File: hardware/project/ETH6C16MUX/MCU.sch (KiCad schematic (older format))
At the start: 32 parts

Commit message: Schematic design
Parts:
- U?: symbol ETH6C12MUX:STM32F765ZGT6 -> ETH6C16MUX:STM32F765ZGT6
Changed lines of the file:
@@
 EESchema Schematic File Version 4
-LIBS:ETH6C12MUX-cache
+LIBS:ETH6C16MUX-cache
 EELAYER 30 0
 EELAYER END
@@
 	7600 10900 7600 10950
 $Comp
-L ETH6C12MUX:+3.3V_MCU #PWR?
+L ETH6C16MUX:+3.3V_MCU #PWR?
 U 1 1 5DA5C116
 P 6700 10450
@@
 $EndComp
 $Comp
-L ETH6C12MUX:+3.3V_MCU #PWR?
+L ETH6C16MUX:+3.3V_MCU #PWR?
 U 1 1 5DBD22D5
 P 850 9200
@@
 $EndComp
 $Comp
-L ETH6C12MUX:+3.3V_MCU #PWR?
+L ETH6C16MUX:+3.3V_MCU #PWR?
 U 1 1 5DE7C3C1
 P 10750 9950
@@
 	3650 6000 2900 6000
 $Comp
-L ETH6C12MUX:+3.3V_MCU #PWR?
+L ETH6C16MUX:+3.3V_MCU #PWR?
 U 1 1 5DA689C0
 P 15150 7550
@@
 	9350 800  9350 850
 $Comp
-L ETH6C12MUX:+3.3V_MCU #PWR?
+L ETH6C16MUX:+3.3V_MCU #PWR?
 U 1 1 5DA4E816
 P 9350 800
@@
 $EndComp
 $Comp
-L ETH6C12MUX:STM32F765ZGT6 U?
+L ETH6C16MUX:STM32F765ZGT6 U?
 U 1 1 5D61C76C
 P 9350 4950
@@
 	8550 10450 8550 10500
 $Comp
-L ETH6C12MUX:+3.3V_MCU #PWR?
+L ETH6C16MUX:+3.3V_MCU #PWR?
 U 1 1 5DA61F58
 P 8550 10450
@@
 	3400 10450 3400 10500
 $Comp
-L ETH6C12MUX:+3.3V_MCU #PWR?
+L ETH6C16MUX:+3.3V_MCU #PWR?
 U 1 1 5DA55A02
 P 3400 10450
@@
 $EndComp
 $Comp
-L ETH6C12MUX:+3.3V_MCU #PWR?
+L ETH6C16MUX:+3.3V_MCU #PWR?
 U 1 1 5DEE379F
 P 1350 3850
@@
 	3500 8700 3650 8700
 $Comp
-L ETH6C12MUX:+3.3V_MCU #PWR?
+L ETH6C16MUX:+3.3V_MCU #PWR?
 U 1 1 5DCB5D39
 P 3150 8700
@@
 	1800 2850 1800 2750
 $Comp
-L ETH6C12MUX:+3.3V_MCU #PWR?
+L ETH6C16MUX:+3.3V_MCU #PWR?
 U 1 1 5DDA95AD
 P 1350 2150
@@
 $EndComp
 $Comp
-L ETH6C12MUX:+3.3V_MCU #PWR?
+L ETH6C16MUX:+3.3V_MCU #PWR?
 U 1 1 5DDAA87C
 P 1850 2850
@@
 I2C_SCL
 $Comp
-L ETH6C12MUX:+3.3V_MCU #PWR?
+L ETH6C16MUX:+3.3V_MCU #PWR?
 U 1 1 5DDCF30A
 P 1350 900

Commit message: FPGA schematic
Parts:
- removed U?: 24LC01, symbol Memory_EEPROM:24LC01
- added C? (x3): 100n, symbol Device:C
- added C?: 47n, symbol Device:C
- added U? (x2): S25FL064L_SOIC, symbol ETH6C16MUX:S25FL064L_SOIC
- added U?: ASDM1-20.000MHZ-LC-T, Oscillator:Oscillator_SMD_Abracon_ASDMB-4Pin_2.5x2.0mm, symbol Oscillator:ASDMB-xxxMHz
- U?: value MCP9804_MSOP -> MCP9804
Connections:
- net labels removed: MCU_SPI4_MISO, MCU_SPI4_MOSI, MCU_SPI4_NSS, MCU_SPI4_SCLK, MCU_SPI5_MISO, MCU_SPI5_NSS, MCU_SPI5_SCLK
- wire segments 206 -> 229
- no-connect marks 4 -> 5
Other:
- moved on the sheet: C?, D?, J?, R?, U?

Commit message: Schematic design
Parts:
- removed C?: 47n, symbol Device:C
- removed D?: LED_ARGB, symbol Device:LED_ARGB
- added D301: RED, symbol Device:LED
- added D302: GREEN, symbol Device:LED
- added D303: BLUE, symbol Device:LED
- added J303: Conn_02x01, Connector_PinHeader_2.54mm:PinHeader_1x02_P2.54mm_Vertical, symbol Connector_Generic:Conn_02x01
- added R301: 220, symbol Device:R
- added R302: 12k1, symbol Device:R
- added R303, R304: 4k7, symbol Device:R
- added R307, R308: 270, Resistor_SMD:R_0603_1608Metric_Pad1.05x0.95mm_HandSolder, symbol Device:R
- added R312: 10k, symbol Device:R
- C301, C302, C303, C306, C307, C308, C309, C310, C311, C312, C313, C314, C315, C316, C317, C318: renamed from C?; footprint (none) -> ETH6C16MXU:C_0603_A_Pad1.05x0.95mm_HandSolder
- J302: renamed from J?; footprint (none) -> Connector_PinHeader_2.54mm:PinHeader_1x02_P2.54mm_Vertical
- R306: renamed from R?; value R -> 270; footprint (none) -> Resistor_SMD:R_0603_1608Metric_Pad1.05x0.95mm_HandSolder
- R309, R310: renamed from R?; footprint (none) -> Resistor_SMD:R_0603_1608Metric_Pad1.05x0.95mm_HandSolder
- R311: renamed from R?; value 12k1 -> 10k
- U304: renamed from U?; footprint (none) -> Package_QFP:TQFP-144_20x20mm_P0.5mm
- gave numbers to parts that had none: 14
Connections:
- net labels added: +3.3V, FPGA1_CBSEL0, FPGA1_CBSEL1, FPGA1_CDONE, FPGA1_CFG_CS, FPGA1_CRESET_B, FPGA1_SPI5_CS, FPGA1_SPI5_MISO, FPGA1_SPI5_MOSI, FPGA1_SPI5_SLCK, FPGA2_CBSEL0, FPGA2_CBSEL1, FPGA2_CDONE, FPGA2_CFG_CS, FPGA2_CRESET_B, FPGA2_SPI4_CS, FPGA2_SPI4_MISO, FPGA2_SPI4_MOSI, FPGA2_SPI4_SLCK, MCU_DEFAULT, MODULE_DETECT
- net labels removed: +3.3V_MCU, FPGA_CBSEL0, FPGA_CBSEL1, FPGA_CDONE, FPGA_CFG_CS, FPGA_CRESET_B, FPGA_SPI3_CS
- wire segments 229 -> 271
- no-connect marks 5 -> 69
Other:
- moved on the sheet: C301, C302, C303, C304, C305, C319, C320, C321, C322, FB301, FB302, J301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

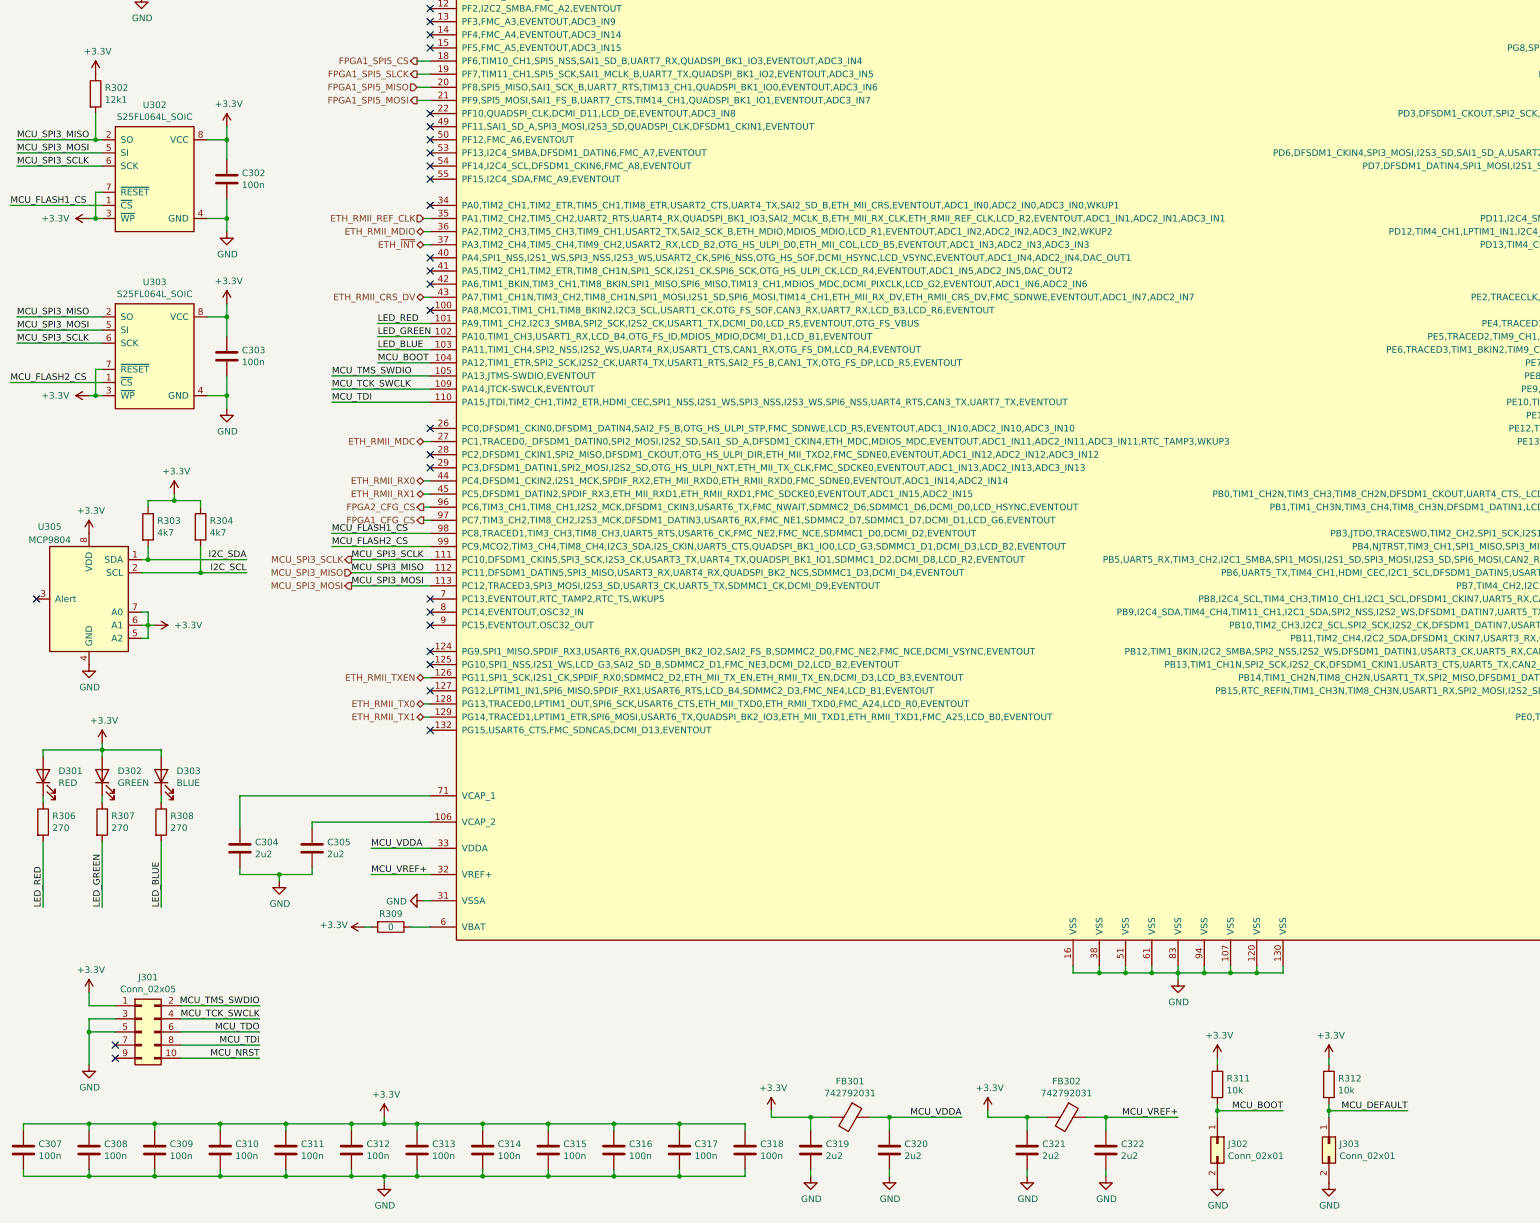
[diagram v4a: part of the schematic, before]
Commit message: PCB design, need to redesign of the board to board connectors.
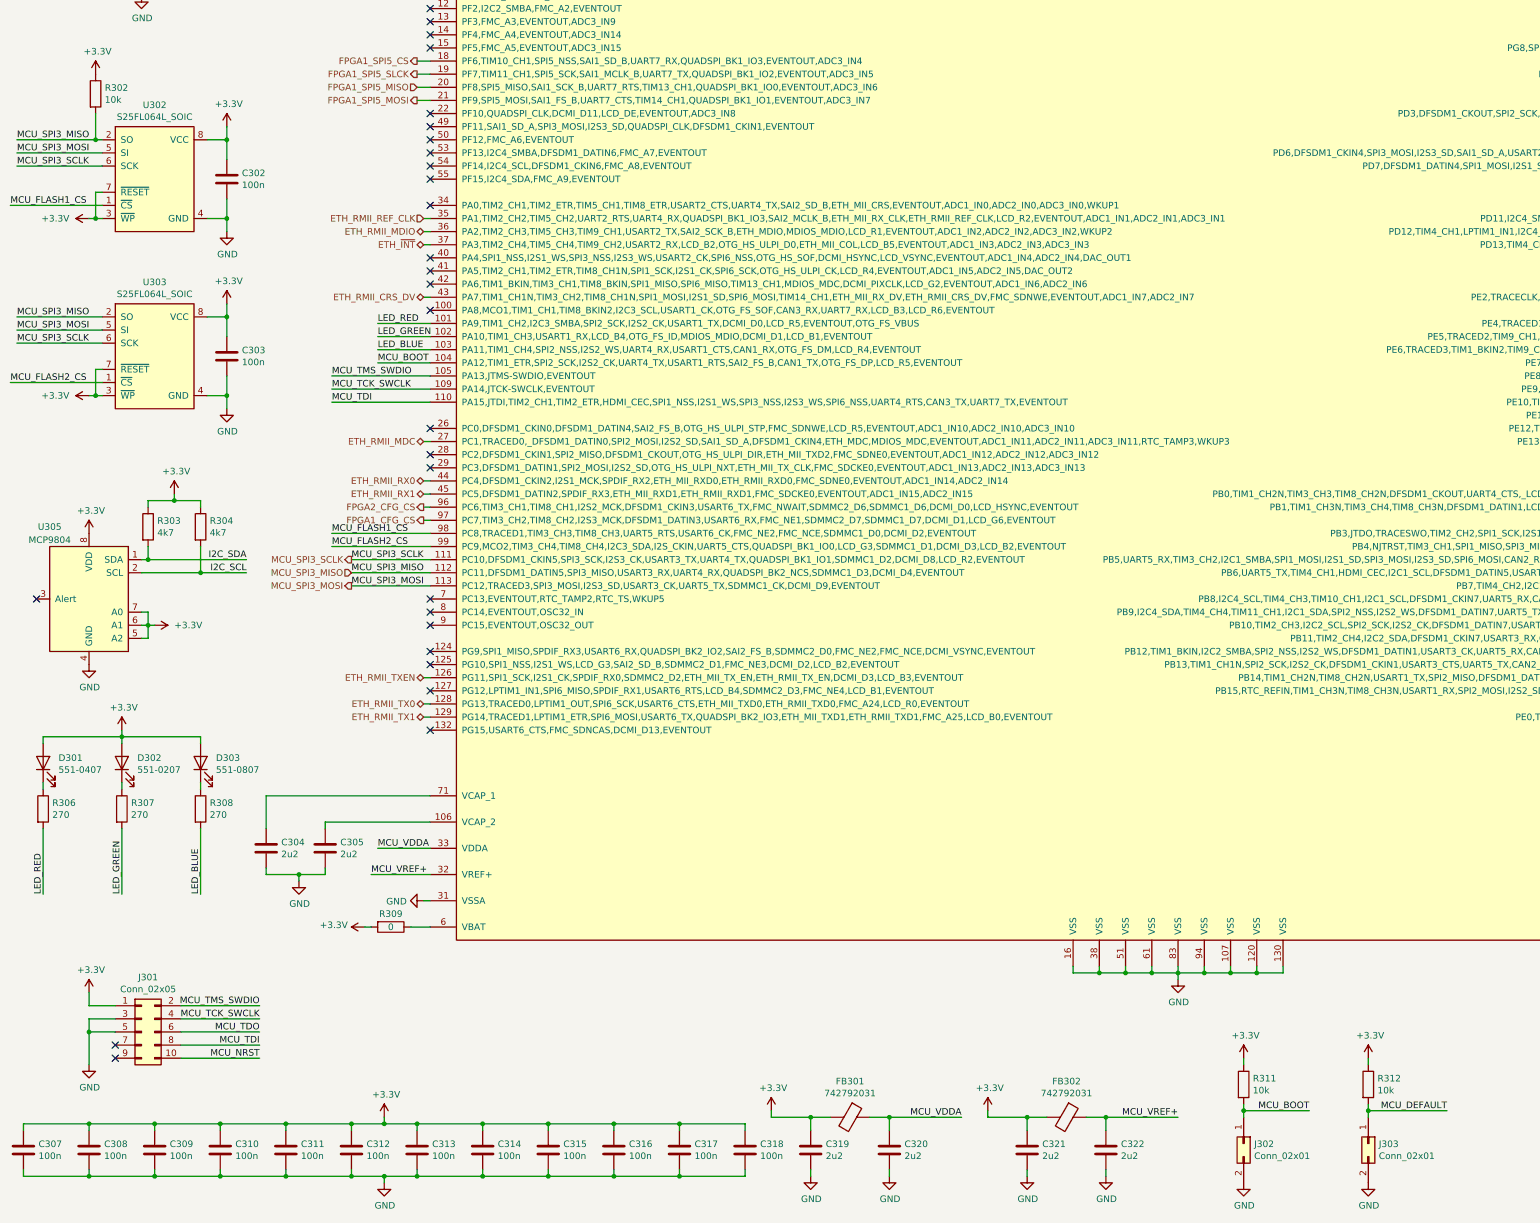
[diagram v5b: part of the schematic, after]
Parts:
- C304, C305, C319, C320, C321, C322: footprint (none) -> ETH6C16MXU:C_0805_C_Pad1.15x1.40mm_HandSolder
- D301: value RED -> 551-0407; footprint (none) -> ETH6C16MXU:551-xx07
- D302: value GREEN -> 551-0207; footprint (none) -> ETH6C16MXU:551-xx07
- D303: value BLUE -> 551-0807; footprint (none) -> ETH6C16MXU:551-xx07
- FB301, FB302: footprint (none) -> ETH6C16MXU:R_0805_D_Pad1.15x1.40mm_HandSolder
- J301: footprint (none) -> Connector_PinHeader_1.27mm:PinHeader_2x05_P1.27mm_Vertical
- R301, R303, R304: footprint (none) -> Resistor_SMD:R_0603_1608Metric_Pad1.05x0.95mm_HandSolder
- R302: value 12k1 -> 10k; footprint (none) -> ETH6C16MXU:R_0603_E_Pad1.05x0.95mm_HandSolder
- R305, R311, R312: footprint (none) -> ETH6C16MXU:R_0603_E_Pad1.05x0.95mm_HandSolder
- R306, R307, R308: footprint Resistor_SMD:R_0603_1608Metric_Pad1.05x0.95mm_HandSolder -> ETH6C16MXU:R_0603_E_Pad1.05x0.95mm_HandSolder
- U302, U303: footprint (none) -> Package_SO:SOIC-8_5.23x5.23mm_P1.27mm
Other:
- moved on the sheet: C304, C305, D301, D302, D303, J302, J303, R306, R307, R308, R311, R312

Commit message: PCB layout, deleted USB.
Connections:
- net MCU_RX_UART3: no longer names the net of U304.70 (PB11,TIM2_CH4,I2C2_SDA,DFSDM1_CKIN7,USART3_RX,OTG_HS_ULPI_D4,ETH_MII_TX_EN,ETH_RMII_TX_EN,_DSI_TE,LCD_G5,EVENTOUT)
- net MCU_TX_UART3: no longer names the net of U304.69 (PB10,TIM2_CH3,I2C2_SCL,SPI2_SCK,I2S2_CK,DFSDM1_DATIN7,USART3_TX,QUADSPI_BK1_NCS,OTG_HS_ULPI_D3,ETH_MII_RX_ER,LCD_G4,EVENTOUT)
- no-connect marks 69 -> 71
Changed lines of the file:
@@
 $Descr A3 16535 11693
 encoding utf-8
-Sheet 3 8
+Sheet 3 7
 Title "MCU"
 Date ""
@@
 Wire Wire Line
 	3700 7100 3750 7100
-Text HLabel 15200 6700 2    50   Output ~ 0
-MCU_TX_UART3
-Text HLabel 15200 6800 2    50   Input ~ 0
-MCU_RX_UART3
-Wire Wire Line
-	15150 6800 15200 6800
-Wire Wire Line
-	15150 6700 15200 6700
 Wire Wire Line
 	3700 5300 3750 5300
@@
 Wire Wire Line
 	2500 8600 2750 8600
+NoConn ~ 15150 6700
+NoConn ~ 15150 6800
 $EndSCHEMATC

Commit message: Deleted FPGA part and change it for SPI IO chips. Change power supply circuit.
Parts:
- removed C319, C320, C321: 2u2, ETH6C16MXU:C_0805_C_Pad1.15x1.40mm_HandSolder, symbol Device:C
- removed D301: 551-0407, ETH6C16MXU:551-xx07, symbol Device:LED
- removed D302: 551-0207, ETH6C16MXU:551-xx07, symbol Device:LED
- removed D303: 551-0807, ETH6C16MXU:551-xx07, symbol Device:LED
- removed FB301: 742792031, ETH6C16MXU:R_0805_D_Pad1.15x1.40mm_HandSolder, symbol Device:Ferrite_Bead
- added C607: 1u, Capacitor_SMD:C_0603_1608Metric_Pad1.05x0.95mm_HandSolder, symbol Device:C
- added D601: 150121M153000, ETH6C16MXU:150121M153000, symbol Device:LED_ARGB
- C601: renamed from C301; footprint ETH6C16MXU:C_0603_A_Pad1.05x0.95mm_HandSolder -> Capacitor_SMD:C_0603_1608Metric_Pad1.05x0.95mm_HandSolder
- C602: renamed from C302; footprint ETH6C16MXU:C_0603_A_Pad1.05x0.95mm_HandSolder -> Capacitor_SMD:C_0603_1608Metric_Pad1.05x0.95mm_HandSolder
- C603: renamed from C303; footprint ETH6C16MXU:C_0603_A_Pad1.05x0.95mm_HandSolder -> Capacitor_SMD:C_0603_1608Metric_Pad1.05x0.95mm_HandSolder
- C604: renamed from C304; footprint ETH6C16MXU:C_0805_C_Pad1.15x1.40mm_HandSolder -> Capacitor_SMD:C_0805_2012Metric_Pad1.15x1.40mm_HandSolder
- C605: renamed from C305; footprint ETH6C16MXU:C_0805_C_Pad1.15x1.40mm_HandSolder -> Capacitor_SMD:C_0805_2012Metric_Pad1.15x1.40mm_HandSolder
- C606: renamed from C306; footprint ETH6C16MXU:C_0603_A_Pad1.05x0.95mm_HandSolder -> Capacitor_SMD:C_0603_1608Metric_Pad1.05x0.95mm_HandSolder
- C608: renamed from C307; footprint ETH6C16MXU:C_0603_A_Pad1.05x0.95mm_HandSolder -> Capacitor_SMD:C_0603_1608Metric_Pad1.05x0.95mm_HandSolder
- C609: renamed from C308; footprint ETH6C16MXU:C_0603_A_Pad1.05x0.95mm_HandSolder -> Capacitor_SMD:C_0603_1608Metric_Pad1.05x0.95mm_HandSolder
- C610: renamed from C309; footprint ETH6C16MXU:C_0603_A_Pad1.05x0.95mm_HandSolder -> Capacitor_SMD:C_0603_1608Metric_Pad1.05x0.95mm_HandSolder
- C611: renamed from C310; footprint ETH6C16MXU:C_0603_A_Pad1.05x0.95mm_HandSolder -> Capacitor_SMD:C_0603_1608Metric_Pad1.05x0.95mm_HandSolder
- C612: renamed from C311; footprint ETH6C16MXU:C_0603_A_Pad1.05x0.95mm_HandSolder -> Capacitor_SMD:C_0603_1608Metric_Pad1.05x0.95mm_HandSolder
- C613: renamed from C312; footprint ETH6C16MXU:C_0603_A_Pad1.05x0.95mm_HandSolder -> Capacitor_SMD:C_0603_1608Metric_Pad1.05x0.95mm_HandSolder
- C614: renamed from C313; footprint ETH6C16MXU:C_0603_A_Pad1.05x0.95mm_HandSolder -> Capacitor_SMD:C_0603_1608Metric_Pad1.05x0.95mm_HandSolder
- C615: renamed from C314; footprint ETH6C16MXU:C_0603_A_Pad1.05x0.95mm_HandSolder -> Capacitor_SMD:C_0603_1608Metric_Pad1.05x0.95mm_HandSolder
- C616: renamed from C315; footprint ETH6C16MXU:C_0603_A_Pad1.05x0.95mm_HandSolder -> Capacitor_SMD:C_0603_1608Metric_Pad1.05x0.95mm_HandSolder
- C617: renamed from C316; footprint ETH6C16MXU:C_0603_A_Pad1.05x0.95mm_HandSolder -> Capacitor_SMD:C_0603_1608Metric_Pad1.05x0.95mm_HandSolder
- C618: renamed from C317; footprint ETH6C16MXU:C_0603_A_Pad1.05x0.95mm_HandSolder -> Capacitor_SMD:C_0603_1608Metric_Pad1.05x0.95mm_HandSolder
- C619: renamed from C318; footprint ETH6C16MXU:C_0603_A_Pad1.05x0.95mm_HandSolder -> Capacitor_SMD:C_0603_1608Metric_Pad1.05x0.95mm_HandSolder
- C620: renamed from C322; value 2u2 -> 1u; footprint ETH6C16MXU:C_0805_C_Pad1.15x1.40mm_HandSolder -> Capacitor_SMD:C_0603_1608Metric_Pad1.05x0.95mm_HandSolder
- FB601: renamed from FB302; footprint ETH6C16MXU:R_0805_D_Pad1.15x1.40mm_HandSolder -> Resistor_SMD:R_0805_2012Metric_Pad1.15x1.40mm_HandSolder
- R602: renamed from R302; footprint ETH6C16MXU:R_0603_E_Pad1.05x0.95mm_HandSolder -> Resistor_SMD:R_0603_1608Metric_Pad1.05x0.95mm_HandSolder
- R605: renamed from R305; footprint ETH6C16MXU:R_0603_E_Pad1.05x0.95mm_HandSolder -> Resistor_SMD:R_0603_1608Metric_Pad1.05x0.95mm_HandSolder
- R606: renamed from R306; value 270 -> 523; footprint ETH6C16MXU:R_0603_E_Pad1.05x0.95mm_HandSolder -> Resistor_SMD:R_0603_1608Metric_Pad1.05x0.95mm_HandSolder
- R607: renamed from R307; value 270 -> 330; footprint ETH6C16MXU:R_0603_E_Pad1.05x0.95mm_HandSolder -> Resistor_SMD:R_0603_1608Metric_Pad1.05x0.95mm_HandSolder
- R608: renamed from R308; value 270 -> 330; footprint ETH6C16MXU:R_0603_E_Pad1.05x0.95mm_HandSolder -> Resistor_SMD:R_0603_1608Metric_Pad1.05x0.95mm_HandSolder
- R611: renamed from R311; footprint ETH6C16MXU:R_0603_E_Pad1.05x0.95mm_HandSolder -> Resistor_SMD:R_0603_1608Metric_Pad1.05x0.95mm_HandSolder
- R612: renamed from R312; footprint ETH6C16MXU:R_0603_E_Pad1.05x0.95mm_HandSolder -> Resistor_SMD:R_0603_1608Metric_Pad1.05x0.95mm_HandSolder
- renumbered J301 to J601, J302 to J602, J303 to J603, R301 to R601, R303 to R603, R304 to R604, R309 to R609, R310 to R610, U301 to U601, U302 to U602, U303 to U603, U304 to U604, U305 to U605
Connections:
- net MCU_VREF+ is gone; now on net MCU_VDDA: C620.1, FB601.1, U604.32 (VREF+)
- net +3V3: now also D601.1 (A)
- net GND: now also C607.2
- net I2C_SCL: now also U604.54 (PF14,I2C4_SCL,DFSDM1_CKIN6,FMC_A8,EVENTOUT); no longer U604.11 (PF1,I2C2_SCL,FMC_A1,EVENTOUT)
- net I2C_SDA: now also U604.55 (PF15,I2C4_SDA,FMC_A9,EVENTOUT); no longer U604.10 (PF0,I2C2_SDA,FMC_A0,EVENTOUT)
- net RELAY1_~RST: now reaches U604.15 (PF5,FMC_A5,EVENTOUT,ADC3_IN15)
- net RELAY2_~RST: now reaches U604.2 (PE3,TRACED0,SAI1_SD_B,FMC_A19,EVENTOUT)
- net RELAY1_~CS0: now reaches U604.22 (PF10,QUADSPI_CLK,DCMI_D11,LCD_DE,EVENTOUT,ADC3_IN8)
- net MODULE_DETECT1: now reaches U604.47 (PB1,TIM1_CH3N,TIM3_CH4,TIM8_CH3N,DFSDM1_DATIN1,LCD_R6,OTG_HS_ULPI_D2,ETH_MII_RXD3,LCD_G0,EVENTOUT,ADC1_IN9,ADC2_IN9)
- net RELAY1_~CS1: now reaches U604.49 (PF11,SAI1_SD_A,SPI3_MOSI,I2S3_SD,QUADSPI_CLK,DFSDM1_CKIN1,EVENTOUT)
- net RELAY1_~CS2: now reaches U604.50 (PF12,FMC_A6,EVENTOUT)
- net RELAY1_~CS3: now reaches U604.53 (PF13,I2C4_SMBA,DFSDM1_DATIN6,FMC_A7,EVENTOUT)
- net at R609.1, U604.6 (VBAT): now also C607.1
- net RELAY2_~CS0: now reaches U604.7 (PC13,EVENTOUT,RTC_TAMP2,RTC_TS,WKUP5)
- net RELAY2_~CS1: now reaches U604.8 (PC14,EVENTOUT,OSC32_IN)
- net RELAY2_~CS2: now reaches U604.9 (PC15,EVENTOUT,OSC32_OUT)
- net at R606.1: now also D601.2 (RK)
- net at R607.1: now also D601.3 (GK)
- net at R608.1: now also D601.4 (BK)
- net FPGA1_CBSEL0: no longer names the net of U604.139 (PB8,I2C4_SCL,TIM4_CH3,TIM10_CH1,I2C1_SCL,DFSDM1_CKIN7,UART5_RX,CAN1_RX,SDMMC2_D4,ETH_MII_TXD3,SDMMC1_D4,DCMI_D6,LCD_B6,EVENTOUT)
- net FPGA1_CBSEL1: no longer names the net of U604.140 (PB9,I2C4_SDA,TIM4_CH4,TIM11_CH1,I2C1_SDA,SPI2_NSS,I2S2_WS,DFSDM1_DATIN7,UART5_TX,CAN1_TX,SDMMC2_D5,I2C4_SMBA,SDMMC1_D5,DCMI_D7,LCD_B7,EVENTOUT)
- net FPGA1_CDONE: no longer names the net of U604.134 (PB4,NJTRST,TIM3_CH1,SPI1_MISO,SPI3_MISO,SPI2_NSS,I2S2_WS,SPI6_MISO,SDMMC2_D3,CAN3_TX,UART7_TX,EVENTOUT)
- net FPGA1_CFG_CS: no longer names the net of U604.97 (PC7,TIM3_CH2,TIM8_CH2,I2S3_MCK,DFSDM1_DATIN3,USART6_RX,FMC_NE1,SDMMC2_D7,SDMMC1_D7,DCMI_D1,LCD_G6,EVENTOUT)
- net FPGA1_CRESET_B: no longer names the net of U604.135 (PB5,UART5_RX,TIM3_CH2,I2C1_SMBA,SPI1_MOSI,I2S1_SD,SPI3_MOSI,I2S3_SD,SPI6_MOSI,CAN2_RX,OTG_HS_ULPI_D7,ETH_PPS_OUT,FMC_SDCKE1,DCMI_D10,LCD_G7,EVENTOUT)
- net FPGA1_SPI5_CS: no longer names the net of U604.18 (PF6,TIM10_CH1,SPI5_NSS,SAI1_SD_B,UART7_RX,QUADSPI_BK1_IO3,EVENTOUT,ADC3_IN4)
- net FPGA1_SPI5_MISO renamed RELAY1_SO
- net FPGA1_SPI5_MOSI renamed RELAY1_SI
- net FPGA1_SPI5_SLCK renamed RELAY1_SCLK
- net FPGA2_CBSEL0: no longer names the net of U604.67 (PE14,TIM1_CH4,SPI4_MOSI,SAI2_MCLK_B,FMC_D11,LCD_CLK,EVENTOUT)
- net FPGA2_CBSEL1: no longer names the net of U604.68 (PE15,TIM1_BKIN,FMC_D12,LCD_R7,EVENTOUT)
- net FPGA2_CDONE: no longer names the net of U604.65 (PE12,TIM1_CH3N,SPI4_SCK,DFSDM1_DATIN5,SAI2_SCK_B,FMC_D9,LCD_B4,EVENTOUT)
- net FPGA2_CFG_CS: no longer names the net of U604.96 (PC6,TIM3_CH1,TIM8_CH1,I2S2_MCK,DFSDM1_CKIN3,USART6_TX,FMC_NWAIT,SDMMC2_D6,SDMMC1_D6,DCMI_D0,LCD_HSYNC,EVENTOUT)
- net FPGA2_CRESET_B: no longer names the net of U604.66 (PE13,TIM1_CH3,SPI4_MISO,DFSDM1_CKIN5,SAI2_FS_B,FMC_D10,LCD_DE,EVENTOUT)
- net FPGA2_SPI4_CS: no longer names the net of U604.3 (PE4,TRACED1,SPI4_NSS,SAI1_FS_A,DFSDM1_DATIN3,FMC_A20,DCMI_D4,LCD_B0,EVENTOUT)
- net FPGA2_SPI4_MISO renamed RELAY2_SO
- net FPGA2_SPI4_MOSI renamed RELAY2_SI
- net FPGA2_SPI4_SLCK renamed RELAY2_SCLK
- net MODULE_DETECT renamed MODULE_DETECT0
- new net RELAY2_~CS3: U604.10 (PF0,I2C2_SDA,FMC_A0,EVENTOUT)
- no-connect marks 71 -> 72
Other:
- moved on the sheet: C620, FB601, J601, J602, J603, R606, R607, R608, R609, R611, R612
